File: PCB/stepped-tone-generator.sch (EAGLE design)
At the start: 35 parts, among them U1 NE555P, U2 NE556N, U3 CD4017BE

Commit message: Made PCB larger. Set proper values for pots.
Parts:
- C1, C2: value 10nF -> 0.01uF
- C4: value 1uF -> 0.01uF
- VOLUME: value 10K -> 1K LOG
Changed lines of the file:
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@@
 <part name="U$1" library="frames-custom" library_urn="urn:adsk.eagle:library:11820551" deviceset="LETTER_L-CIRCUITMONKEY" device="">
 <attribute name="DOCUMENT_NUMBER" value="Stepped Tone Generator with 4-step Sequencer"/>
-<attribute name="REV" value="A"/>
+<attribute name="REV" value="B"/>
 </part>
 <part name="U2" library="logic" library_urn="urn:adsk.eagle:library:8032508" deviceset="556" device="PDIP" package3d_urn="urn:adsk.eagle:package:8032593/4" value="NE556N">
@@
 <part name="R3" library="rlc" library_urn="urn:adsk.eagle:library:4192893" deviceset="RESISTOR" device="THD_0.25_WATT" package3d_urn="urn:adsk.eagle:package:26222947/3" value="1K"/>
 <part name="SUPPLY10" library="supply" library_urn="urn:adsk.eagle:library:10485988" deviceset="VCC" device=""/>
-<part name="C1" library="rlc" library_urn="urn:adsk.eagle:library:4192893" deviceset="CAPACITOR" device="THD_5MM" package3d_urn="urn:adsk.eagle:package:4192947/2" value="10nF"/>
-<part name="C2" library="rlc" library_urn="urn:adsk.eagle:library:4192893" deviceset="CAPACITOR" device="THD_5MM" package3d_urn="urn:adsk.eagle:package:4192947/2" value="10nF"/>
+<part name="C1" library="rlc" library_urn="urn:adsk.eagle:library:4192893" deviceset="CAPACITOR" device="THD_5MM" package3d_urn="urn:adsk.eagle:package:4192947/2" value="0.01uF"/>
+<part name="C2" library="rlc" library_urn="urn:adsk.eagle:library:4192893" deviceset="CAPACITOR" device="THD_5MM" package3d_urn="urn:adsk.eagle:package:4192947/2" value="0.01uF"/>
 <part name="SUPPLY11" library="supply" library_urn="urn:adsk.eagle:library:10485988" deviceset="GND" device=""/>
 <part name="SUPPLY12" library="supply" library_urn="urn:adsk.eagle:library:10485988" deviceset="GND" device=""/>
@@
 <part name="SUPPLY21" library="supply" library_urn="urn:adsk.eagle:library:10485988" deviceset="GND" device=""/>
 <part name="SUPPLY22" library="supply" library_urn="urn:adsk.eagle:library:10485988" deviceset="GND" device=""/>
-<part name="PWR_AUX" library="con-headers" library_urn="urn:adsk.eagle:library:5539071" deviceset="CON_03X1" device="-2.54MM-THD-VT" package3d_urn="urn:adsk.eagle:package:7887260/1" value="3P, Male, Breakaway, 2.54mm"/>
+<part name="PWR_AUX" library="con-headers" library_urn="urn:adsk.eagle:library:5539071" deviceset="CON_03X1" device="-2.54MM-THD-VT" package3d_urn="urn:adsk.eagle:package:7887260/3" value="3P, Male, Breakaway, 2.54mm"/>
 <part name="SUPPLY25" library="supply" library_urn="urn:adsk.eagle:library:10485988" deviceset="GND" device=""/>
-<part name="C4" library="rlc" library_urn="urn:adsk.eagle:library:4192893" deviceset="CAPACITOR" device="THD_5MM" package3d_urn="urn:adsk.eagle:package:4192947/2" value="1uF"/>
+<part name="C4" library="rlc" library_urn="urn:adsk.eagle:library:4192893" deviceset="CAPACITOR" device="THD_5MM" package3d_urn="urn:adsk.eagle:package:4192947/2" value="0.01uF"/>
 <part name="C3" library="rlc" library_urn="urn:adsk.eagle:library:4192893" deviceset="CAPACITOR" device="THD_5MM" package3d_urn="urn:adsk.eagle:package:4192947/2" value="10uF"/>
 <part name="SUPPLY20" library="supply" library_urn="urn:adsk.eagle:library:10485988" deviceset="VCC" device=""/>
@@
 <part name="R7" library="rlc" library_urn="urn:adsk.eagle:library:4192893" deviceset="RESISTOR" device="THD_0.25_WATT" package3d_urn="urn:adsk.eagle:package:26222947/3" value="1K"/>
 <part name="SUPPLY23" library="supply" library_urn="urn:adsk.eagle:library:10485988" deviceset="VCC" device=""/>
-<part name="VOLUME" library="rlc" library_urn="urn:adsk.eagle:library:4192893" deviceset="POT" device="RK09?113" package3d_urn="urn:adsk.eagle:package:9396884/2" value="10K"/>
-<part name="TONE1" library="rlc" library_urn="urn:adsk.eagle:library:4192893" deviceset="POT" device="RK09?113" package3d_urn="urn:adsk.eagle:package:9396884/2" value="500K"/>
-<part name="TONE2" library="rlc" library_urn="urn:adsk.eagle:library:4192893" deviceset="POT" device="RK09?113" package3d_urn="urn:adsk.eagle:package:9396884/2" value="500K"/>
-<part name="SPEED" library="rlc" library_urn="urn:adsk.eagle:library:4192893" deviceset="POT" device="RK09?113" package3d_urn="urn:adsk.eagle:package:9396884/2" value="500K"/>
-<part name="TRIM1" library="rlc" library_urn="urn:adsk.eagle:library:4192893" deviceset="POT" device="RK09?113" package3d_urn="urn:adsk.eagle:package:9396884/2" value="100K"/>
-<part name="TRIM2" library="rlc" library_urn="urn:adsk.eagle:library:4192893" deviceset="POT" device="RK09?113" package3d_urn="urn:adsk.eagle:package:9396884/2" value="100K"/>
-<part name="TRIM3" library="rlc" library_urn="urn:adsk.eagle:library:4192893" deviceset="POT" device="RK09?113" package3d_urn="urn:adsk.eagle:package:9396884/2" value="100K"/>
-<part name="TRIM4" library="rlc" library_urn="urn:adsk.eagle:library:4192893" deviceset="POT" device="RK09?113" package3d_urn="urn:adsk.eagle:package:9396884/2" value="100K"/>
+<part name="VOLUME" library="rlc" library_urn="urn:adsk.eagle:library:4192893" deviceset="POT" device="RK09?113" package3d_urn="urn:adsk.eagle:package:9396884/3" value="1K LOG"/>
+<part name="TONE1" library="rlc" library_urn="urn:adsk.eagle:library:4192893" deviceset="POT" device="RK09?113" package3d_urn="urn:adsk.eagle:package:9396884/3" value="500K"/>
+<part name="TONE2" library="rlc" library_urn="urn:adsk.eagle:library:4192893" deviceset="POT" device="RK09?113" package3d_urn="urn:adsk.eagle:package:9396884/3" value="500K"/>
+<part name="SPEED" library="rlc" library_urn="urn:adsk.eagle:library:4192893" deviceset="POT" device="RK09?113" package3d_urn="urn:adsk.eagle:package:9396884/3" value="500K"/>
+<part name="TRIM1" library="rlc" library_urn="urn:adsk.eagle:library:4192893" deviceset="POT" device="RK09?113" package3d_urn="urn:adsk.eagle:package:9396884/3" value="100K"/>
+<part name="TRIM2" library="rlc" library_urn="urn:adsk.eagle:library:4192893" deviceset="POT" device="RK09?113" package3d_urn="urn:adsk.eagle:package:9396884/3" value="100K"/>
+<part name="TRIM3" library="rlc" library_urn="urn:adsk.eagle:library:4192893" deviceset="POT" device="RK09?113" package3d_urn="urn:adsk.eagle:package:9396884/3" value="100K"/>
+<part name="TRIM4" library="rlc" library_urn="urn:adsk.eagle:library:4192893" deviceset="POT" device="RK09?113" package3d_urn="urn:adsk.eagle:package:9396884/3" value="100K"/>
 </parts>
 <sheets>

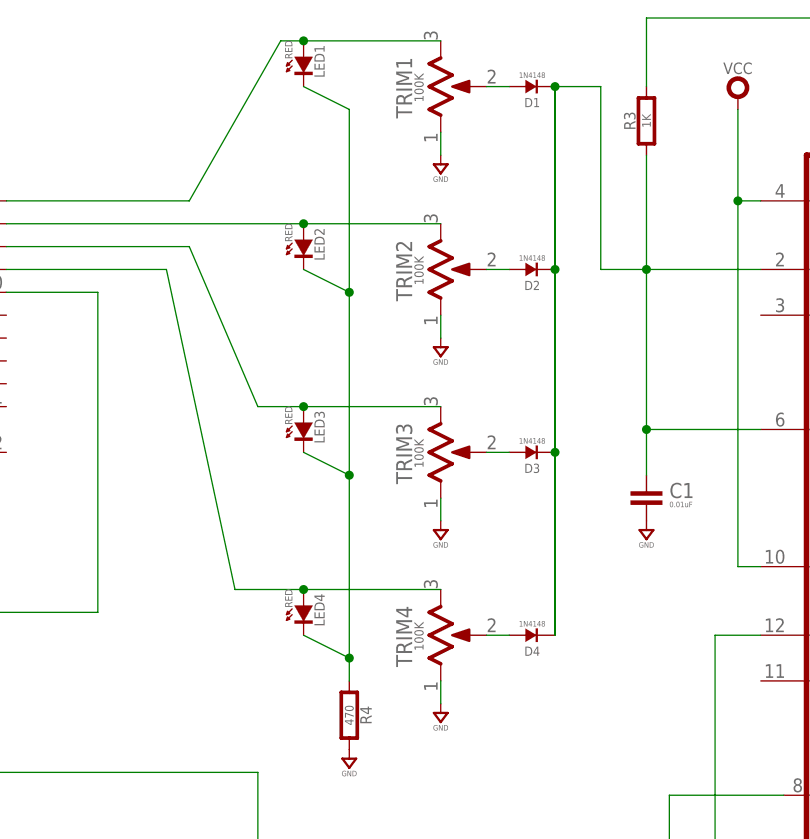
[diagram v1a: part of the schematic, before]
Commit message: Added labels for pots.
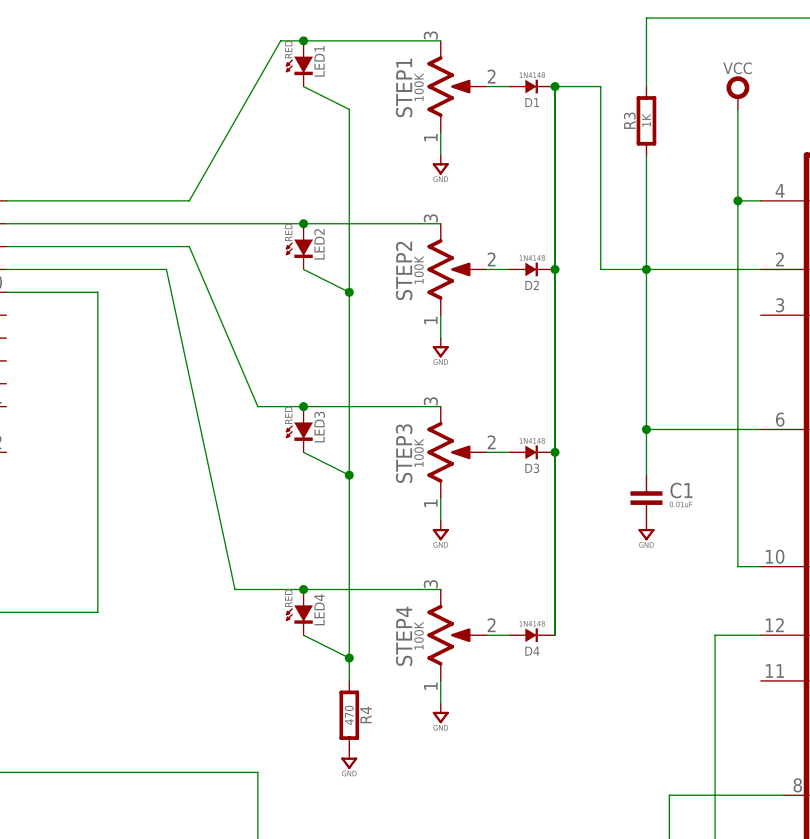
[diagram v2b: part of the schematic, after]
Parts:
- renumbered TRIM1 to STEP1, TRIM2 to STEP2, TRIM3 to STEP3, TRIM4 to STEP4
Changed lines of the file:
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@@
 <part name="TONE2" library="rlc" library_urn="urn:adsk.eagle:library:4192893" deviceset="POT" device="RK09?113" package3d_urn="urn:adsk.eagle:package:9396884/3" value="500K"/>
 <part name="SPEED" library="rlc" library_urn="urn:adsk.eagle:library:4192893" deviceset="POT" device="RK09?113" package3d_urn="urn:adsk.eagle:package:9396884/3" value="500K"/>
-<part name="TRIM1" library="rlc" library_urn="urn:adsk.eagle:library:4192893" deviceset="POT" device="RK09?113" package3d_urn="urn:adsk.eagle:package:9396884/3" value="100K"/>
-<part name="TRIM2" library="rlc" library_urn="urn:adsk.eagle:library:4192893" deviceset="POT" device="RK09?113" package3d_urn="urn:adsk.eagle:package:9396884/3" value="100K"/>
-<part name="TRIM3" library="rlc" library_urn="urn:adsk.eagle:library:4192893" deviceset="POT" device="RK09?113" package3d_urn="urn:adsk.eagle:package:9396884/3" value="100K"/>
-<part name="TRIM4" library="rlc" library_urn="urn:adsk.eagle:library:4192893" deviceset="POT" device="RK09?113" package3d_urn="urn:adsk.eagle:package:9396884/3" value="100K"/>
+<part name="STEP1" library="rlc" library_urn="urn:adsk.eagle:library:4192893" deviceset="POT" device="RK09?113" package3d_urn="urn:adsk.eagle:package:9396884/3" value="100K"/>
+<part name="STEP2" library="rlc" library_urn="urn:adsk.eagle:library:4192893" deviceset="POT" device="RK09?113" package3d_urn="urn:adsk.eagle:package:9396884/3" value="100K"/>
+<part name="STEP3" library="rlc" library_urn="urn:adsk.eagle:library:4192893" deviceset="POT" device="RK09?113" package3d_urn="urn:adsk.eagle:package:9396884/3" value="100K"/>
+<part name="STEP4" library="rlc" library_urn="urn:adsk.eagle:library:4192893" deviceset="POT" device="RK09?113" package3d_urn="urn:adsk.eagle:package:9396884/3" value="100K"/>
 </parts>
 <sheets>
@@
 <attribute name="VALUE" x="98.933" y="50.927" size="1.016" layer="96" rot="R270" align="center"/>
 </instance>
-<instance part="TRIM1" gate="POT" x="104.14" y="165.1" smashed="yes" rot="R90">
+<instance part="STEP1" gate="POT" x="104.14" y="165.1" smashed="yes" rot="R90">
 <attribute name="NAME" x="100.076" y="164.973" size="1.778" layer="95" ratio="15" rot="R90" align="center"/>
 <attribute name="VALUE" x="101.727" y="164.973" size="1.016" layer="96" rot="R90" align="center"/>
 </instance>
-<instance part="TRIM2" gate="POT" x="104.14" y="144.78" smashed="yes" rot="R90">
+<instance part="STEP2" gate="POT" x="104.14" y="144.78" smashed="yes" rot="R90">
 <attribute name="NAME" x="100.076" y="144.653" size="1.778" layer="95" ratio="15" rot="R90" align="center"/>
 <attribute name="VALUE" x="101.727" y="144.653" size="1.016" layer="96" rot="R90" align="center"/>
 </instance>
-<instance part="TRIM3" gate="POT" x="104.14" y="124.46" smashed="yes" rot="R90">
+<instance part="STEP3" gate="POT" x="104.14" y="124.46" smashed="yes" rot="R90">
 <attribute name="NAME" x="100.076" y="124.333" size="1.778" layer="95" ratio="15" rot="R90" align="center"/>
 <attribute name="VALUE" x="101.727" y="124.333" size="1.016" layer="96" rot="R90" align="center"/>
 </instance>
-<instance part="TRIM4" gate="POT" x="104.14" y="104.14" smashed="yes" rot="R90">
+<instance part="STEP4" gate="POT" x="104.14" y="104.14" smashed="yes" rot="R90">
 <attribute name="NAME" x="100.076" y="104.013" size="1.778" layer="95" ratio="15" rot="R90" align="center"/>
 <attribute name="VALUE" x="101.727" y="104.013" size="1.016" layer="96" rot="R90" align="center"/>
@@
 </segment>
 <segment>
-<pinref part="TRIM1" gate="POT" pin="1"/>
+<pinref part="STEP1" gate="POT" pin="1"/>
 <pinref part="SUPPLY14" gate="GND" pin="GND"/>
 <wire x1="104.14" y1="160.02" x2="104.14" y2="157.48" width="0.1524" layer="91"/>
 </segment>
 <segment>
-<pinref part="TRIM2" gate="POT" pin="1"/>
+<pinref part="STEP2" gate="POT" pin="1"/>
 <pinref part="SUPPLY16" gate="GND" pin="GND"/>
 <wire x1="104.14" y1="139.7" x2="104.14" y2="137.16" width="0.1524" layer="91"/>
 </segment>
 <segment>
-<pinref part="TRIM3" gate="POT" pin="1"/>
+<pinref part="STEP3" gate="POT" pin="1"/>
 <pinref part="SUPPLY17" gate="GND" pin="GND"/>
 <wire x1="104.14" y1="119.38" x2="104.14" y2="116.84" width="0.1524" layer="91"/>
 </segment>
 <segment>
-<pinref part="TRIM4" gate="POT" pin="1"/>
+<pinref part="STEP4" gate="POT" pin="1"/>
 <pinref part="SUPPLY18" gate="GND" pin="GND"/>
 <wire x1="104.14" y1="99.06" x2="104.14" y2="96.52" width="0.1524" layer="91"/>
@@
 <wire x1="86.36" y1="170.18" x2="88.9" y2="170.18" width="0.1524" layer="91"/>
 <pinref part="LED1" gate="G$1" pin="A"/>
-<pinref part="TRIM1" gate="POT" pin="3"/>
+<pinref part="STEP1" gate="POT" pin="3"/>
 <wire x1="88.9" y1="170.18" x2="104.14" y2="170.18" width="0.1524" layer="91"/>
 <junction x="88.9" y="170.18"/>
@@
 <wire x1="55.88" y1="149.86" x2="88.9" y2="149.86" width="0.1524" layer="91"/>
 <pinref part="LED2" gate="G$1" pin="A"/>
-<pinref part="TRIM2" gate="POT" pin="3"/>
+<pinref part="STEP2" gate="POT" pin="3"/>
 <wire x1="88.9" y1="149.86" x2="104.14" y2="149.86" width="0.1524" layer="91"/>
 <junction x="88.9" y="149.86"/>
@@
 <wire x1="83.82" y1="129.54" x2="88.9" y2="129.54" width="0.1524" layer="91"/>
 <pinref part="LED3" gate="G$1" pin="A"/>
-<pinref part="TRIM3" gate="POT" pin="3"/>
+<pinref part="STEP3" gate="POT" pin="3"/>
 <wire x1="88.9" y1="129.54" x2="104.14" y2="129.54" width="0.1524" layer="91"/>
 <junction x="88.9" y="129.54"/>
@@
 <wire x1="81.28" y1="109.22" x2="88.9" y2="109.22" width="0.1524" layer="91"/>
 <pinref part="LED4" gate="G$1" pin="A"/>
-<pinref part="TRIM4" gate="POT" pin="3"/>
+<pinref part="STEP4" gate="POT" pin="3"/>
 <wire x1="88.9" y1="109.22" x2="104.14" y2="109.22" width="0.1524" layer="91"/>
 <junction x="88.9" y="109.22"/>
@@
 <pinref part="D1" gate="G$1" pin="A"/>
 <wire x1="111.76" y1="165.1" x2="109.22" y2="165.1" width="0.1524" layer="91"/>
-<pinref part="TRIM1" gate="POT" pin="2"/>
+<pinref part="STEP1" gate="POT" pin="2"/>
 </segment>
 </net>
@@
 <pinref part="D2" gate="G$1" pin="A"/>
 <wire x1="111.76" y1="144.78" x2="109.22" y2="144.78" width="0.1524" layer="91"/>
-<pinref part="TRIM2" gate="POT" pin="2"/>
+<pinref part="STEP2" gate="POT" pin="2"/>
 </segment>
 </net>
@@
 <pinref part="D3" gate="G$1" pin="A"/>
 <wire x1="111.76" y1="124.46" x2="109.22" y2="124.46" width="0.1524" layer="91"/>
-<pinref part="TRIM3" gate="POT" pin="2"/>
+<pinref part="STEP3" gate="POT" pin="2"/>
 </segment>
 </net>
@@
 <pinref part="D4" gate="G$1" pin="A"/>
 <wire x1="111.76" y1="104.14" x2="109.22" y2="104.14" width="0.1524" layer="91"/>
-<pinref part="TRIM4" gate="POT" pin="2"/>
-</segment>
-</net>
+<pinref part="STEP4" gate="POT" pin="2"/>
+</segment>
+</net>

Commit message: Stepped tone generator fixes
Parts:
- C4: value 0.01uF -> 1uF
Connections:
- net N$22: now also SPEEDPOT.3; no longer SPEEDPOT.1
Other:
- note added: "0109"
- moved on the sheet: SPEED
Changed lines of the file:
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@@
 <part name="PWR_AUX" library="con-headers" library_urn="urn:adsk.eagle:library:5539071" deviceset="CON_03X1" device="-2.54MM-THD-VT" package3d_urn="urn:adsk.eagle:package:7887260/3" value="3P, Male, Breakaway, 2.54mm"/>
 <part name="SUPPLY25" library="supply" library_urn="urn:adsk.eagle:library:10485988" deviceset="GND" device=""/>
-<part name="C4" library="rlc" library_urn="urn:adsk.eagle:library:4192893" deviceset="CAPACITOR" device="THD_5MM" package3d_urn="urn:adsk.eagle:package:4192947/2" value="0.01uF"/>
+<part name="C4" library="rlc" library_urn="urn:adsk.eagle:library:4192893" deviceset="CAPACITOR" device="THD_5MM" package3d_urn="urn:adsk.eagle:package:4192947/2" value="1uF"/>
 <part name="C3" library="rlc" library_urn="urn:adsk.eagle:library:4192893" deviceset="CAPACITOR" device="THD_5MM" package3d_urn="urn:adsk.eagle:package:4192947/2" value="10uF"/>
 <part name="SUPPLY20" library="supply" library_urn="urn:adsk.eagle:library:10485988" deviceset="VCC" device=""/>
@@
 connect both sources, smoke might
 happen.  Voltage range 5-9 volts.</text>
+<text x="234.188" y="6.858" size="5.588" layer="97" ratio="15" align="bottom-right">0109</text>
 </plain>
 <instances>
@@
 <attribute name="SHEET" x="233.68" y="1.27" size="2.54" layer="94" font="vector"/>
 <attribute name="DRAWING_NAME" x="91.44" y="1.27" size="2.54" layer="94" font="vector" ratio="15"/>
-<attribute name="DOCUMENT_NUMBER" x="154.94" y="6.096" size="2.54" layer="94" ratio="15"/>
+<attribute name="DOCUMENT_NUMBER" x="149.86" y="6.096" size="2.032" layer="94" ratio="15"/>
 <attribute name="REV" x="241.808" y="8.382" size="3.81" layer="94" ratio="15" align="center"/>
 </instance>
@@
 <attribute name="VALUE" x="243.713" y="155.067" size="1.016" layer="96" rot="R270" align="center"/>
 </instance>
-<instance part="SPEED" gate="POT" x="96.52" y="50.8" smashed="yes" rot="R270">
-<attribute name="NAME" x="100.584" y="50.927" size="1.778" layer="95" ratio="15" rot="R270" align="center"/>
-<attribute name="VALUE" x="98.933" y="50.927" size="1.016" layer="96" rot="R270" align="center"/>
+<instance part="SPEED" gate="POT" x="96.52" y="50.8" smashed="yes" rot="MR90">
+<attribute name="NAME" x="100.584" y="50.673" size="1.778" layer="95" ratio="15" rot="MR90" align="center"/>
+<attribute name="VALUE" x="98.933" y="50.673" size="1.016" layer="96" rot="MR90" align="center"/>
 </instance>
 <instance part="STEP1" gate="POT" x="104.14" y="165.1" smashed="yes" rot="R90">
@@
 </segment>
 </net>
-<net name="N$22" class="0">
-<segment>
-<wire x1="96.52" y1="55.88" x2="96.52" y2="58.42" width="0.1524" layer="91"/>
-<pinref part="R7" gate="G$1" pin="1"/>
-<pinref part="SPEED" gate="POT" pin="1"/>
-</segment>
-</net>
 <net name="N$24" class="0">
 <segment>
@@
 </segment>
 </net>
+<net name="N$22" class="0">
+<segment>
+<pinref part="SPEED" gate="POT" pin="3"/>
+<pinref part="R7" gate="G$1" pin="1"/>
+<wire x1="96.52" y1="55.88" x2="96.52" y2="58.42" width="0.1524" layer="91"/>
+</segment>
+</net>
